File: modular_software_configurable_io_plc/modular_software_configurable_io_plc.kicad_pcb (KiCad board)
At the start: 4 copper layers, 105 x 107 mm, 35 parts, among them J1 FW-14-03-G-D-085-155, J10 CLP-108-02-G-D-BE, J11 CLP-102-02-G-D-BE, J12 CLP-102-02-G-D-BE, J13 CLP-102-02-G-D-BE, J14 CLP-108-02-G-D-BE, J15 FW-14-03-G-D-085-155, J16 FW-02-03-G-D-085-155, J17 FW-02-03-G-D-085-155, J18 FW-02-03-G-D-085-155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

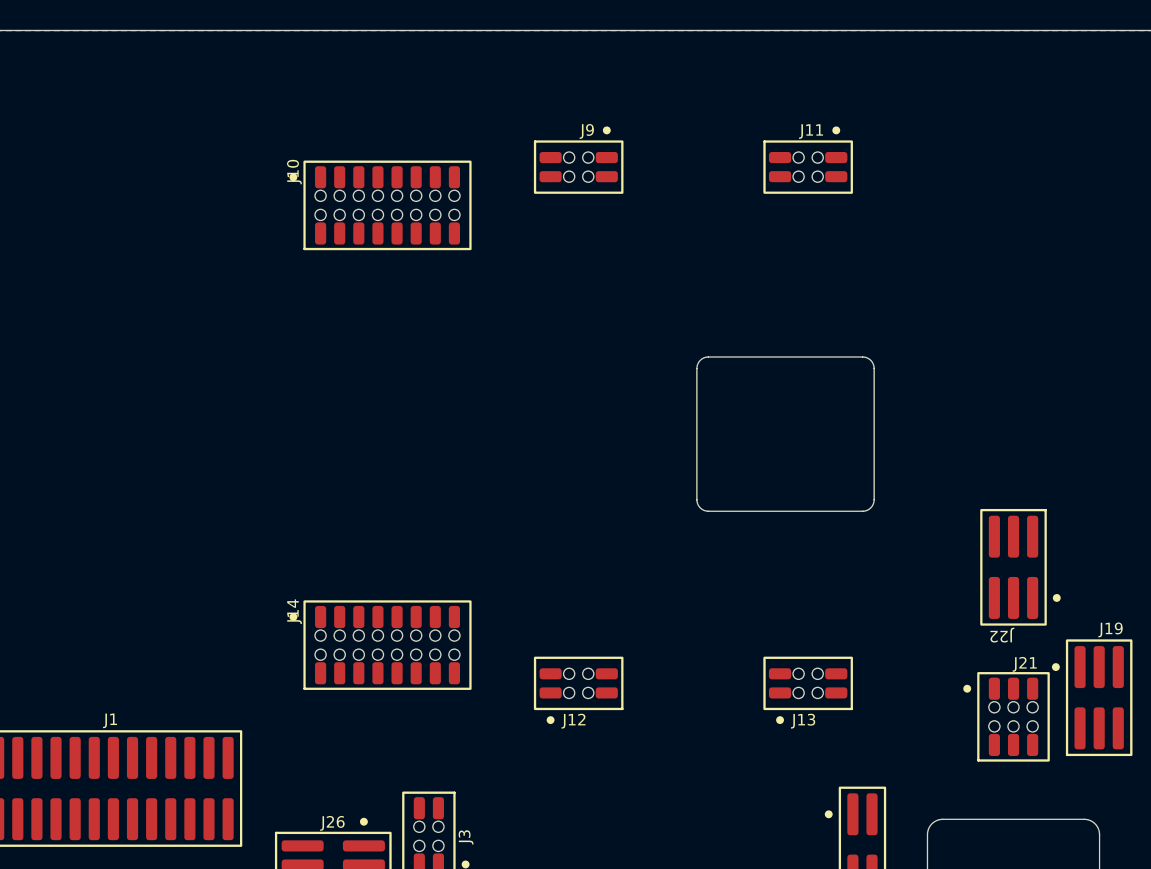
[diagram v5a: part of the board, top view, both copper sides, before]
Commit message: Update KiCAD Symbol Generator submodule to latest commit
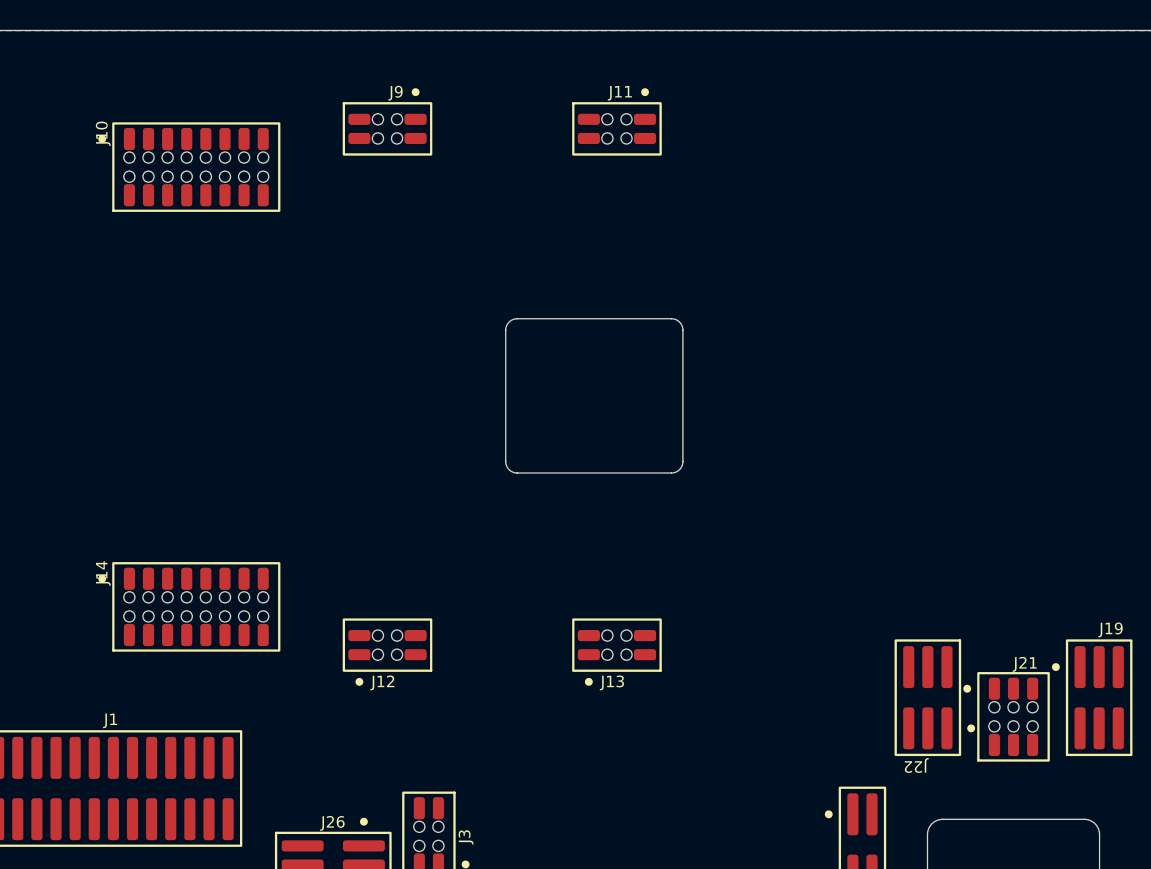
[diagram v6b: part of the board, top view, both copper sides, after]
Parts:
- moved J11 13.0 mm to (188.8, 46.7)
- moved J12 13.0 mm to (173.5, 81.0)
- moved J13 13.0 mm to (188.8, 81.0)
- moved J9 13.0 mm to (173.5, 46.7)
- moved J10 13.0 mm to (160.8, 49.3)
- moved MOD3 13.0 mm to (178.6, 63.9)
- moved J14 13.0 mm to (160.8, 78.5)
- moved J22 10.4 mm to (209.4, 84.5)
- moved MOD6 8.36 mm to (212.0, 66.8)
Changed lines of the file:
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@@
 	(footprint "modules_footprints:minimal_adp1032"
 		(layer "F.Cu")
-		(at 191.28232 66.421)
+		(at 178.58232 63.881)
 		(property "Reference" "MOD3"
 			(at 0.00508 0 0)
@@
 	(footprint "connector_footprints:FW-03-03-G-D-085-155"
 		(layer "F.Cu")
-		(at 215.10752 75.8571 180)
+		(at 209.41792 84.5185 180)
 		(property "Reference" "J22"
 			(at 0 -4.572 180)
@@
 		)
 		(property "Footprint" "connector_footprints:FW-03-03-G-D-085-155"
-			(at 0 0 360)
+			(at 0 0 0)
 			(layer "F.Fab")
 			(hide yes)
@@
 		)
 		(property "Datasheet" "https://suddendocs.samtec.com/catalog_english/fw_sm.pdf?_gl=1*1xtxv9c*_gcl_au*MTM0MTYyNTQ5MS4xNzM2MDk5MTUz*_ga*MTYxNDYyMTQ0Mi4xNzM2MDk5MTUz*_ga_3KFNZC07WW*MTczODE2NTI0NS4zMi4xLjE3MzgxNjU1NjMuNjAuMC4w"
-			(at 0 0 360)
+			(at 0 0 0)
 			(layer "F.Fab")
 			(hide yes)
@@
 		)
 		(property "Description" "Samtec FW-xx-03-G-D-085-155 series,  3 positions connector,  1.27 mm pitch,  Black,  Vertical mounting,  5.2 A,  300 V,  Surface Mount,  Gold plated"
-			(at 0 0 360)
+			(at 0 0 0)
 			(layer "F.Fab")
 			(hide yes)
@@
 	(footprint "connector_footprints:CLP-102-02-G-D-BE"
 		(layer "F.Cu")
-		(at 201.46772 83.566 90)
+		(at 188.76772 81.026 90)
 		(property "Reference" "J13"
 			(at -2.44 -1.085 0)
@@
 	(footprint "connector_footprints:CLP-102-02-G-D-BE"
 		(layer "F.Cu")
-		(at 201.46772 49.276 -90)
+		(at 188.76772 46.736 -90)
 		(property "Reference" "J11"
 			(at -2.44 -1.085 0)
@@
 	(footprint "connector_footprints:CLP-108-02-G-D-BE"
 		(layer "F.Cu")
-		(at 173.52772 51.816)
+		(at 160.82772 49.276)
 		(property "Reference" "J10"
 			(at -6.25 -1.455 90)
@@
 	(footprint "connector_footprints:CLP-108-02-G-D-BE"
 		(layer "F.Cu")
-		(at 173.52772 81.026)
+		(at 160.82772 78.486)
 		(property "Reference" "J14"
 			(at -6.25 -1.455 90)
@@
 	(footprint "connector_footprints:CLP-102-02-G-D-BE"
 		(layer "F.Cu")
-		(at 186.22772 83.566 90)
+		(at 173.52772 81.026 90)
 		(property "Reference" "J12"
 			(at -2.44 -1.085 0)
@@
 	(footprint "connector_footprints:CLP-102-02-G-D-BE"
 		(layer "F.Cu")
-		(at 186.22772 49.276 -90)
+		(at 173.52772 46.736 -90)
 		(property "Reference" "J9"
 			(at -2.44 -1.085 0)
@@
 	(footprint "modules_footprints:minimal_spoe_hybrid"
 		(layer "F.Cu")
-		(at 217.64752 60.6425 -90)
+		(at 211.95792 66.7639 -90)
 		(property "Reference" "MOD6"
 			(at 0.00254 -0.5 -90)
@@
 		(sheetfile "modular_software_configurable_io_plc.kicad_sch")
 		(fp_line
-			(start 10.795 9.144)
-			(end -18.415 9.144)
+			(start 13.335 9.144)
+			(end -20.955 9.144)
 			(stroke
 				(width 0.05)
@@
 		)
 		(fp_line
-			(start -19.05 8.509)
-			(end -19.05 -8.509)
+			(start -21.59 8.509)
+			(end -21.59 -8.509)
 			(stroke
 				(width 0.05)
@@
 		)
 		(fp_line
-			(start 18.415 6.35)
-			(end 13.335 6.35)
+			(start 20.955 6.35)
+			(end 15.875 6.35)
 			(stroke
 				(width 0.05)
@@
 		)
 		(fp_line
-			(start 11.43 5.715)
-			(end 11.43 8.509)
+			(start 13.97 5.715)
+			(end 13.97 8.509)
 			(stroke
 				(width 0.05)
@@
 		)
 		(fp_line
-			(start 11.43 -0.635)
-			(end 11.43 -8.509)
+			(start 13.97 -0.635)
+			(end 13.97 -4.699)
 			(stroke
 				(width 0.05)
@@
 		)
 		(fp_line
-			(start 19.05 -0.635)
-			(end 19.05 5.715)
+			(start 21.59 -0.635)
+			(end 21.59 5.715)
 			(stroke
 				(width 0.05)
@@
 		)
 		(fp_line
-			(start 13.335 -1.27)
-			(end 18.415 -1.27)
+			(start 15.875 -1.27)
+			(end 20.955 -1.27)
 			(stroke
 				(width 0.05)
@@
 		)
 		(fp_line
-			(start -18.415 -9.144)
-			(end 10.795 -9.144)
+			(start -3.81 -5.334)
+			(end 13.335 -5.334)
+			(stroke
+				(width 0.05)
+				(type default)
+			)
+			(layer "Cmts.User")
+		)
+		(fp_line
+			(start -4.445 -5.969)
+			(end -4.445 -8.509)
+			(stroke
+				(width 0.05)
+				(type default)
+			)
+			(layer "Cmts.User")
+		)
+		(fp_line
+			(start -20.955 -9.144)
+			(end -5.08 -9.144)
 			(stroke
 				(width 0.05)
@@
 		)
 		(fp_arc
-			(start -18.415 9.144)
-			(mid -18.864013 8.958013)
-			(end -19.05 8.509)
+			(start -20.955 9.144)
+			(mid -21.404013 8.958013)
+			(end -21.59 8.509)
 			(stroke
 				(width 0.05)
@@
 		)
 		(fp_arc
-			(start 11.43 8.509)
-			(mid 11.244013 8.958013)
-			(end 10.795 9.144)
+			(start 13.97 8.509)
+			(mid 13.784013 8.958013)
+			(end 13.335 9.144)
 			(stroke
 				(width 0.05)
@@
 		)
 		(fp_arc
-			(start 13.335 6.35)
-			(mid 12.885987 6.164013)
-			(end 12.7 5.715)
+			(start 15.875 6.35)
+			(mid 15.425987 6.164013)
+			(end 15.24 5.715)
 			(stroke
 				(width 0.05)
@@
 		)
 		(fp_arc
-			(start 11.43 5.715)
-			(mid 11.615987 5.265987)
-			(end 12.065 5.08)
+			(start 13.97 5.715)
+			(mid 14.155987 5.265987)
+			(end 14.605 5.08)
 			(stroke
 				(width 0.05)
@@
 		)
 		(fp_arc
-			(start 19.05 5.715)
-			(mid 18.864013 6.164013)
-			(end 18.415 6.35)
+			(start 21.59 5.715)
+			(mid 21.404013 6.164013)
+			(end 20.955 6.35)
 			(stroke
 				(width 0.05)
@@
 		)
 		(fp_arc
-			(start 12.065 5.08)
-			(mid 12.514013 5.265987)
-			(end 12.7 5.715)
+			(start 14.605 5.08)
+			(mid 15.054013 5.265987)
+			(end 15.24 5.715)
+			(stroke
+				(width 0.05)
+				(type default)
+			)
+			(layer "Cmts.User")
+		)
+		(fp_arc
+			(start 14.605 0)
+			(mid 14.155987 -0.185987)
+			(end 13.97 -0.635)
 			(stroke
 				(width 0.05)
@@
 		)
 		(fp_arc
-			(start 12.065 0)
-			(mid 11.615987 -0.185987)
-			(end 11.43 -0.635)
+			(start 15.24 -0.635)
+			(mid 15.054013 -0.185987)
+			(end 14.605 0)
 			(stroke
 				(width 0.05)
@@
 		)
 		(fp_arc
-			(start 12.7 -0.635)
-			(mid 12.514013 -0.185987)
-			(end 12.065 0)
+			(start 15.24 -0.635)
+			(mid 15.425987 -1.084013)
+			(end 15.875 -1.27)
 			(stroke
 				(width 0.05)
@@
 		)
 		(fp_arc
-			(start 12.7 -0.635)
-			(mid 12.885987 -1.084013)
-			(end 13.335 -1.27)
+			(start 20.955 -1.27)
+			(mid 21.404013 -1.084013)
+			(end 21.59 -0.635)
 			(stroke
 				(width 0.05)
@@
 		)
 		(fp_arc
-			(start 18.415 -1.27)
-			(mid 18.864013 -1.084013)
-			(end 19.05 -0.635)
+			(start -3.81 -5.334)
+			(mid -4.259013 -5.519987)
+			(end -4.445 -5.969)
 			(stroke
 				(width 0.05)
@@
 		)
 		(fp_arc
-			(start -19.05 -8.509)
-			(mid -18.864013 -8.958013)
-			(end -18.415 -9.144)
+			(start 13.335 -5.334)
+			(mid 13.784013 -5.148013)
+			(end 13.97 -4.699)
 			(stroke
 				(width 0.05)
@@
 		)
 		(fp_arc
-			(start 10.795 -9.144)
-			(mid 11.244013 -8.958013)
-			(end 11.43 -8.509)
+			(start -21.59 -8.509)
+			(mid -21.404013 -8.958013)
+			(end -20.955 -9.144)
+			(stroke
+				(width 0.05)
+				(type default)
+			)
+			(layer "Cmts.User")
+		)
+		(fp_arc
+			(start -5.08 -9.144)
+			(mid -4.630987 -8.958013)
+			(end -4.445 -8.509)
 			(stroke
 				(width 0.05)
@@
 		)
 		(fp_circle
-			(center 15.2146 2.54)
-			(end 15.7226 2.54)
+			(center 17.7546 2.54)
+			(end 18.2626 2.54)
 			(stroke
 				(width 0.0254)
@@
 		)
 		(property "Footprint" "connector_footprints:CLP-103-02-G-D-BE"
-			(at 0 0 360)
+			(at 0 0 0)
 			(layer "F.Fab")
 			(hide yes)
@@
 		)
 		(property "Datasheet" "https://suddendocs.samtec.com/catalog_english/clp_sm.pdf?_gl=1*1y4jlr9*_gcl_au*MTM0MTYyNTQ5MS4xNzM2MDk5MTUz*_ga*MTYxNDYyMTQ0Mi4xNzM2MDk5MTUz*_ga_3KFNZC07WW*MTczNjY4MDQ4OS4xNS4xLjE3MzY2ODEzNzcuNjAuMC4w"
-			(at 0 0 360)
+			(at 0 0 0)
 			(layer "F.Fab")
 			(hide yes)
@@
 		)
 		(property "Description" "Samtec CLP-1xx-02-G-D-BE series,  3 positions connector,  1.27 mm pitch,  Black,  Vertical mounting,  5.2 A,  300 V,  Surface Mount,  Tin plated"
-			(at 0 0 360)
+			(at 0 0 0)
 			(layer "F.Fab")
 			(hide yes)

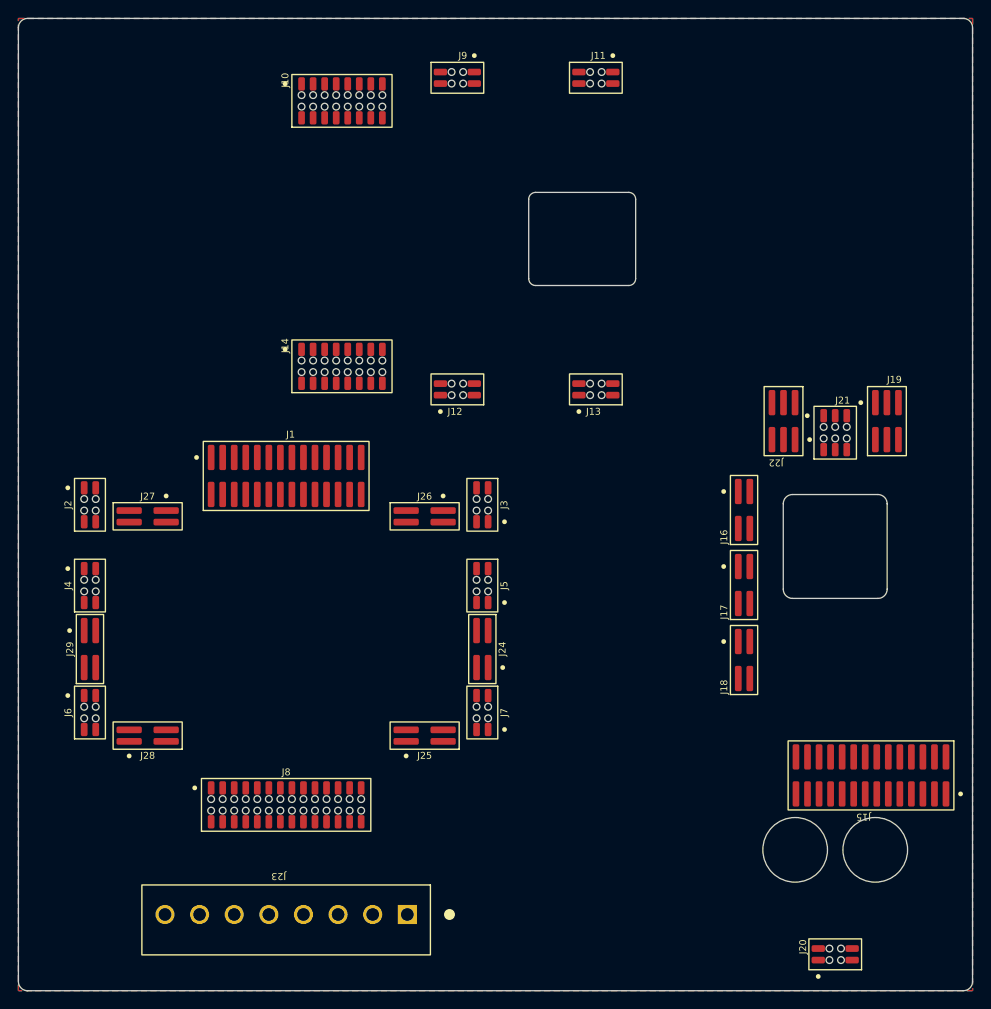
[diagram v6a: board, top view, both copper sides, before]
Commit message: Update KiCAD Symbol Generator submodule and add new footprint and symbol libraries
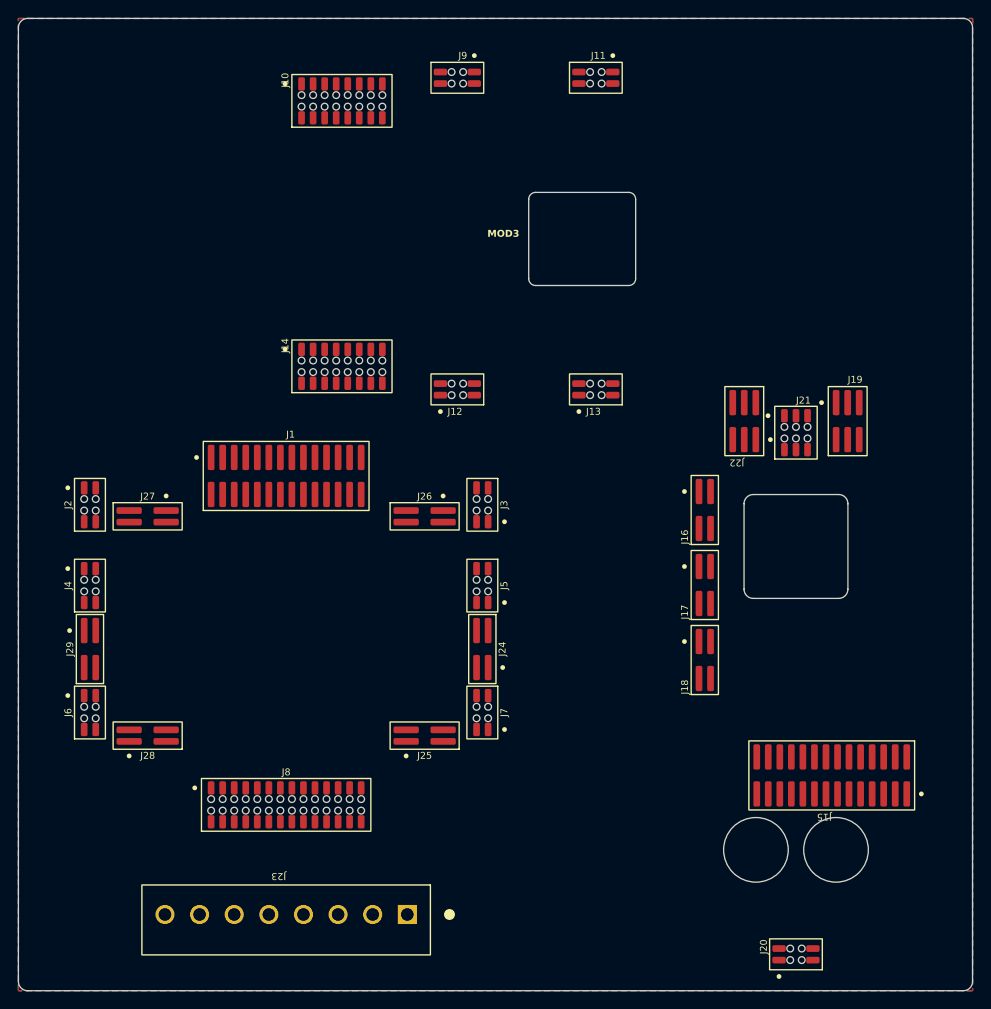
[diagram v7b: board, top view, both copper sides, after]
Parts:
- added M1: ~, mechanical_parts:2907525, F.Cu at (177.7, 93.7)
- added M2: ~, mechanical_parts:2959696, F.Cu at (127.7, 93.7)
- added M3: ~, mechanical_parts:2959683, F.Cu at (227.7, 93.7)
- J23: value TBP02R2-381-08BE -> TBP02R2-381
- moved J15 4.32 mm to (214.7, 123.5)
- moved J16 4.32 mm to (200.8, 94.3)
- moved J17 4.32 mm to (200.8, 102.6)
- moved J18 4.32 mm to (200.8, 110.8)
- moved J19 4.32 mm to (216.5, 84.5)
- moved J22 4.32 mm to (205.1, 84.5)
- moved MOD6 4.32 mm to (207.6, 66.8)
- moved J20 4.32 mm to (210.8, 143.2)
- moved J21 4.32 mm to (210.8, 85.8)
- moved MOD4 4.32 mm to (211.6, 104.1)
- moved MOD5 4.32 mm to (210.8, 115.3)

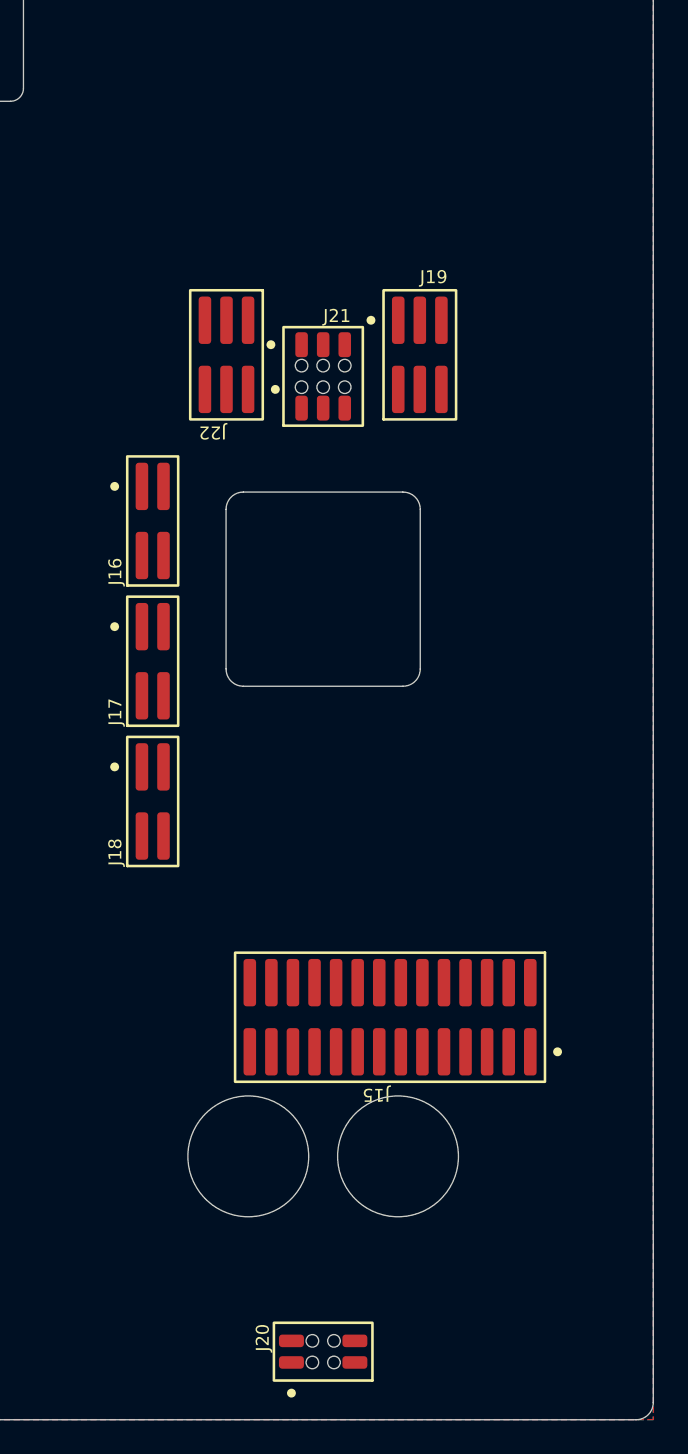
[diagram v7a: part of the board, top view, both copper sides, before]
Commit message: Update KiCAD Symbol Generator submodule to latest commit
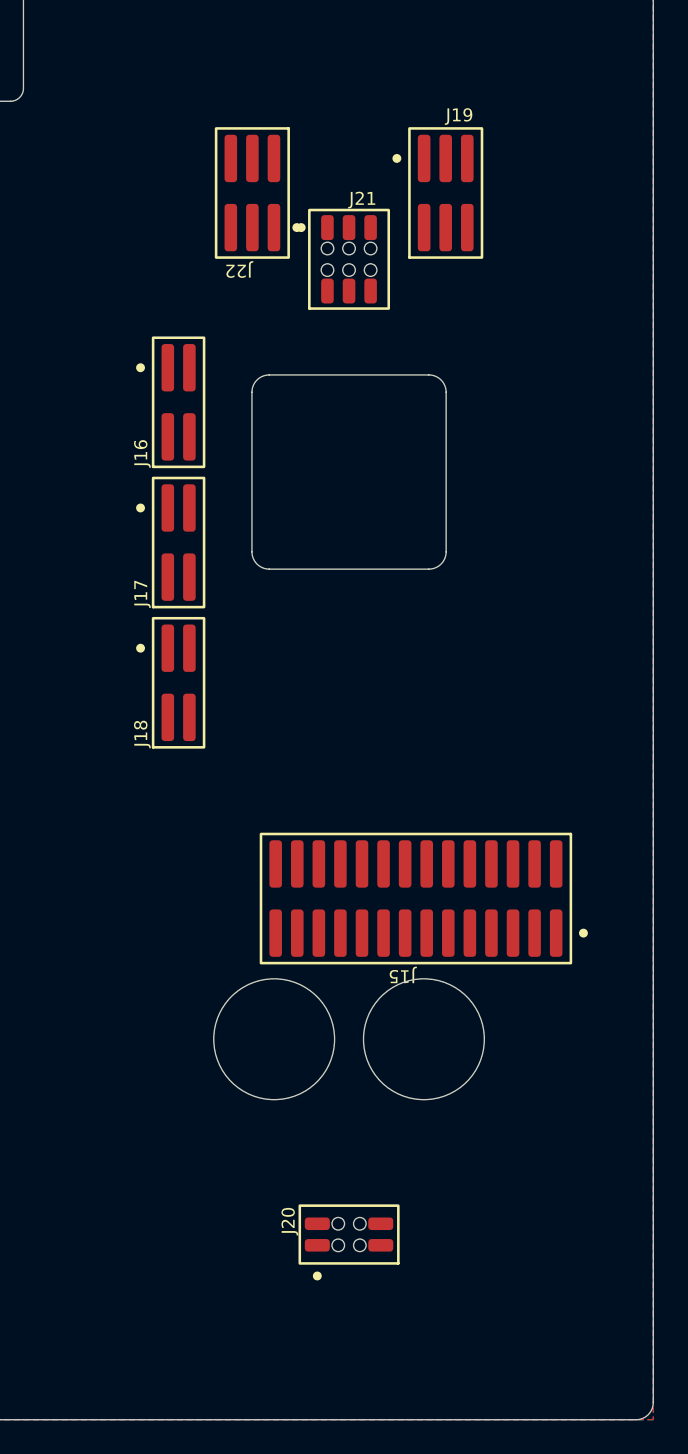
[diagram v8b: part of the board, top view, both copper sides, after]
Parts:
- moved J19 9.65 mm to (218.0, 75.0)
- moved J22 9.65 mm to (206.6, 75.0)
- moved MOD4 8.39 mm to (213.1, 95.9)
- moved MOD6 7.90 mm to (212.3, 60.4)
- moved J15 7.15 mm to (216.3, 116.5)
- moved J16 7.15 mm to (202.3, 87.3)
- moved J17 7.15 mm to (202.3, 95.6)
- moved J18 7.15 mm to (202.3, 103.8)
- moved J20 7.06 mm to (212.3, 136.3)
- moved MOD5 7.06 mm to (212.3, 108.4)
- moved J21 7.06 mm to (212.3, 78.9)
